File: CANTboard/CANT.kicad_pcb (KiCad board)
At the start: 2 copper layers, 20 x 50 mm, 25 parts, among them P1 SWD, P2 CAN, P3 USB, U1 STM32F042C6T6, U2 MCP2562-E/SN, U3 LD1117S33TR, U4 74LVC1G66

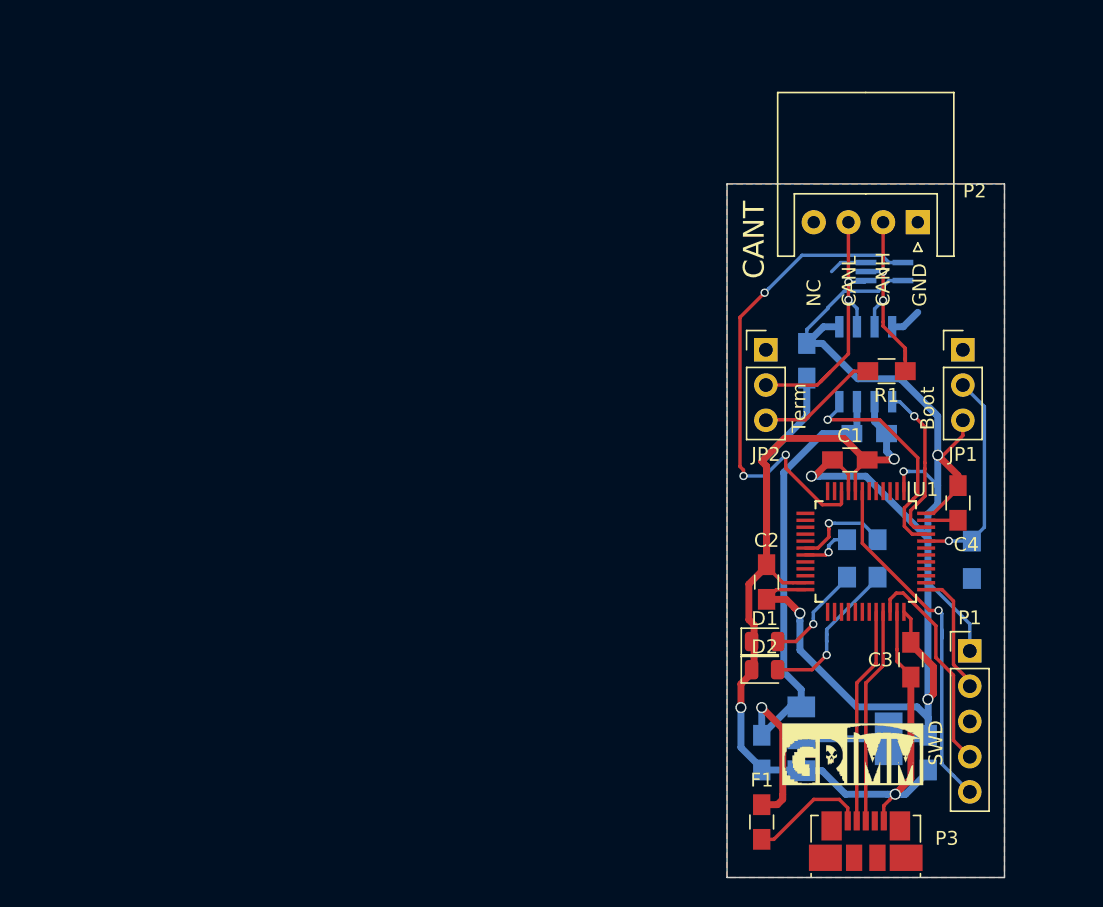
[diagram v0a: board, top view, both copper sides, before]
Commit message: Laid out CANT board based on STM32H7
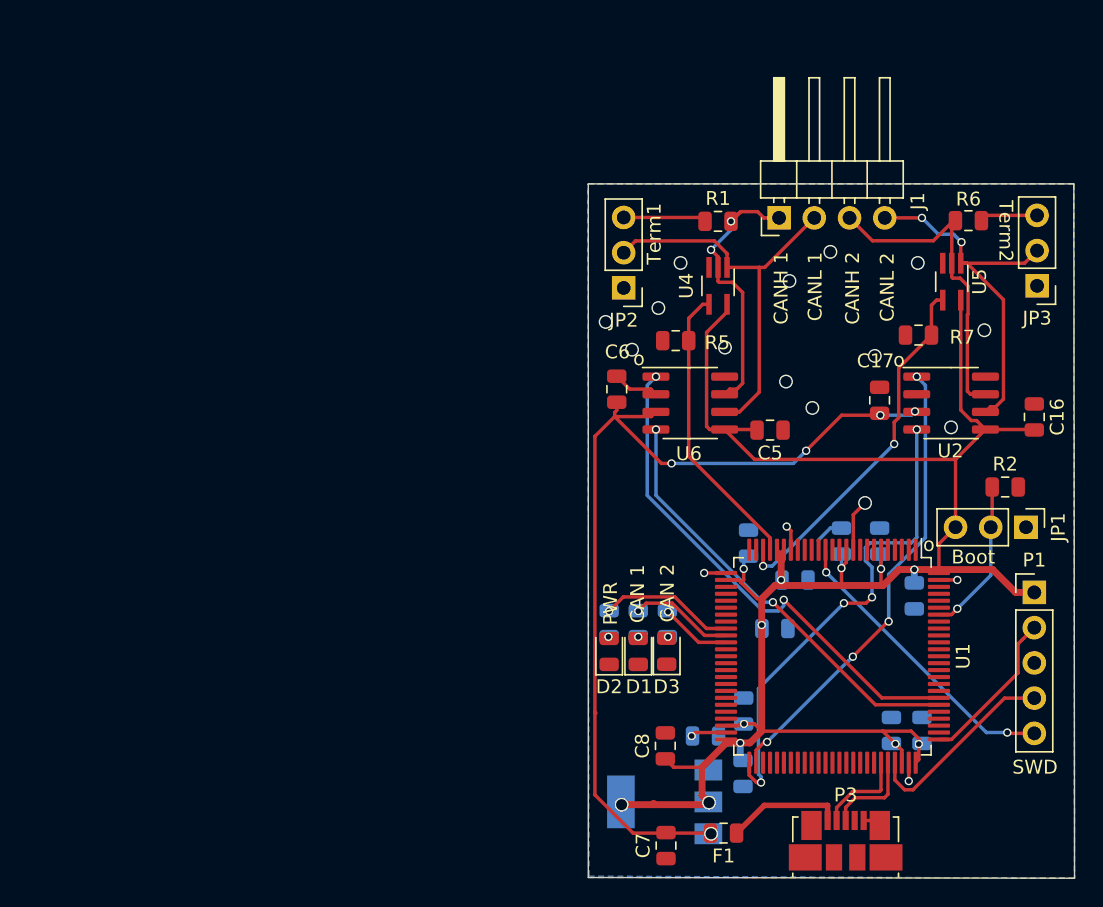
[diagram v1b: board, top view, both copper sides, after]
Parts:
- removed G***: LOGO, LOGO
- removed P2: CAN, Connectors_JST:JST_XH_S04B-XH-A_04x2.50mm_Angled
- added C10: 2.2uF, Capacitor_SMD:C_0805_2012Metric, B.Cu at (133.6, 116.9)
- added C11: 100nF, Capacitor_SMD:C_0805_2012Metric, B.Cu at (122.9, 120.0)
- added C12: 100nF, Capacitor_SMD:C_0805_2012Metric, B.Cu at (135.8, 116.9)
- added C13: 100nF, Capacitor_SMD:C_0805_2012Metric, B.Cu at (135.2, 107.2)
- added C14: 100nF, Capacitor_SMD:C_0805_2012Metric, B.Cu at (126.7, 106.0)
- added C15: 1uF, Capacitor_SMD:C_0805_2012Metric, B.Cu at (125.2, 109.5)
- added C16: 100nF, Capacitor_SMD:C_0805_2012Metric, F.Cu at (143.9, 94.3)
- added C17: 100nF, Capacitor_SMD:C_0805_2012Metric, F.Cu at (132.8, 93.1)
- added C9: 2.2uF, Capacitor_SMD:C_0805_2012Metric, B.Cu at (123.0, 115.5)
- added D3: LED-RED, LED_SMD:LED_0805_2012Metric, F.Cu at (117.4, 111.2)
- added J1: Screw_Terminal_01x04, Connector_PinHeader_2.54mm:PinHeader_1x04_P2.54mm_Horizontal, F.Cu at (125.5, 80.0)
- added JP3: Jumper_NC_Dual, Connector_PinHeader_2.54mm:PinHeader_1x03_P2.54mm_Vertical, F.Cu at (144.1, 84.8)
- added R5: 4.7K, Resistor_SMD:R_0805_2012Metric, F.Cu at (118.0, 88.8)
- added R6: 120, Resistor_SMD:R_0805_2012Metric, F.Cu at (139.2, 80.2)
- added R7: 4.7K, Resistor_SMD:R_0805_2012Metric, F.Cu at (135.6, 88.4)
- added R8: 68, Resistor_SMD:R_0805_2012Metric, B.Cu at (117.5, 109.2)
- added U5: 74LVC1G66, Package_TO_SOT_SMD:SOT-353_SC-70-5_Handsoldering, F.Cu at (137.9, 84.5)
- added U6: MCP2558FD-xSN, Package_SO:SOIC-8_3.9x4.9mm_P1.27mm, F.Cu at (119.1, 93.3)
- C1, C2, C4: value 0.1uF -> 100nF; footprint Capacitors_SMD:C_0805_HandSoldering -> Capacitor_SMD:C_0805_2012Metric; moved to B.Cu
- C3: value 1uF -> 4.7uF; footprint Capacitors_SMD:C_0805_HandSoldering -> Capacitor_SMD:C_0805_2012Metric; moved to B.Cu
- C5, C6: value 0.1uF -> 100nF; footprint Capacitors_SMD:C_0805_HandSoldering -> Capacitor_SMD:C_0805_2012Metric; moved to F.Cu
- C7, C8: footprint Capacitors_SMD:C_0805_HandSoldering -> Capacitor_SMD:C_0805_2012Metric; moved to F.Cu
- F1: footprint Capacitors_SMD:C_0805_HandSoldering -> Capacitor_SMD:C_0805_2012Metric
- JP1, JP2: footprint Pin_Headers:Pin_Header_Straight_1x03_Pitch2.54mm -> Connector_PinHeader_2.54mm:PinHeader_1x03_P2.54mm_Vertical
- P1: footprint Pin_Headers:Pin_Header_Straight_1x05_Pitch2.54mm -> Connector_PinHeader_2.54mm:PinHeader_1x05_P2.54mm_Vertical
- P3: footprint Connectors_Molex:USB_Micro-B_Molex_47346-0001 -> Connector_USB:USB_Micro-B_Molex_47346-0001
- R1: footprint Resistors_SMD:R_0805_HandSoldering -> Resistor_SMD:R_0805_2012Metric
- R2: footprint Resistors_SMD:R_0805_HandSoldering -> Resistor_SMD:R_0805_2012Metric; moved to F.Cu
- R3, R4: value R -> 68; footprint Resistors_SMD:R_0805_HandSoldering -> Resistor_SMD:R_0805_2012Metric
- U1: value STM32F042C6T6 -> STM32H743VITx; footprint Housings_QFP:LQFP-48_7x7mm_Pitch0.5mm -> Package_QFP:LQFP-100_14x14mm_P0.5mm
- U2: value MCP2562-E/SN -> MCP2558FD-xSN; footprint Housings_SOIC:SOIC-8_3.9x4.9mm_Pitch1.27mm -> Package_SO:SOIC-8_3.9x4.9mm_P1.27mm; moved to F.Cu
- U4: moved to F.Cu
- moved R4 19.9 mm to (113.2, 109.2)
- moved C8 19.0 mm to (117.3, 118.0), turned to 90 degrees
- moved R1 16.3 mm to (121.1, 80.2)
- moved C3 15.8 mm to (120.2, 117.3), turned to 180 degrees
- moved R3 15.8 mm to (115.3, 109.2)
- moved C4 15.4 mm to (123.3, 103.4), turned to 90 degrees
- moved C6 13.9 mm to (113.8, 92.3), turned to 270 degrees
- moved U3 13.8 mm to (117.2, 122.0), turned to 180 degrees
- moved JP1 13.6 mm to (143.3, 102.2), turned to 270 degrees
- moved U4 12.0 mm to (121.1, 84.8), turned to 270 degrees
- moved D2 11.3 mm to (113.2, 111.2), turned to 90 degrees
- moved JP2 11.2 mm to (114.3, 85.0), turned to 180 degrees
- moved C7 9.62 mm to (117.3, 125.2)
- moved D1 9.14 mm to (115.3, 111.2), turned to 90 degrees
- moved U1 7.92 mm to (129.3, 111.5)
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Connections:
- C5 pad 2: VBUS -> VCC
- C6 pad 2: VCC -> VBUS
- JP1 pad 1: Net-(JP1-Pad1) -> (no net)
- JP2 pad 1: Net-(JP2-Pad1) -> (no net)
- JP2 pad 2: CAN_L -> CAN1_L
- P3 pad 4: Net-(P3-Pad4) -> (no net)
- R1 pad 2: CAN_H -> CAN1_H
- R3 pad 2: LED_ACT -> LED_ACT1
- R4 pad 2: LED_PWR -> LED_PWR1
- U1 pad 1: VCC -> (no net)
- U1 pad 10: CAN_SHORT -> GND
- U1 pad 11: Net-(U1-Pad11) -> VCC
- U1 pad 12: Net-(U1-Pad12) -> (no net)
- U1 pad 13: Net-(U1-Pad13) -> (no net)
- U1 pad 14: Net-(U1-Pad14) -> /NRST
- U1 pad 15: Net-(U1-Pad15) -> (no net)
- U1 pad 16: Net-(U1-Pad16) -> (no net)
- U1 pad 17: Net-(U1-Pad17) -> (no net)
- U1 pad 18: LED_PWR -> (no net)
- U1 pad 19: LED_ACT -> GND
- U1 pad 2: Net-(U1-Pad2) -> (no net)
- U1 pad 20: Net-(U1-Pad20) -> VCC
- U1 pad 21: Net-(U1-Pad21) -> VCC
- U1 pad 22: Net-(U1-Pad22) -> CAN1_SHORT
- U1 pad 23: GND -> CAN2_SHORT
- U1 pad 24: VCC -> (no net)
- U1 pad 25: Net-(U1-Pad25) -> (no net)
- U1 pad 26: Net-(U1-Pad26) -> GND
- U1 pad 27: Net-(U1-Pad27) -> VCC
- U1 pad 28: Net-(U1-Pad28) -> (no net)
- U1 pad 29: Net-(U1-Pad29) -> (no net)
- U1 pad 3: Net-(U1-Pad3) -> (no net)
- U1 pad 30: Net-(U1-Pad30) -> (no net)
- U1 pad 31: Net-(U1-Pad31) -> (no net)
- U1 pad 32: /USB_DM -> (no net)
- U1 pad 33: /USB_DP -> (no net)
- U1 pad 34: /SWDIO -> LED_PWR1
- U1 pad 35: GND -> LED_ACT1
- U1 pad 36: VCC -> LED_ACT2
- U1 pad 37: /SWCLK -> (no net)
- U1 pad 38: Net-(U1-Pad38) -> (no net)
- U1 pad 39: Net-(U1-Pad39) -> (no net)
- U1 pad 4: Net-(U1-Pad4) -> (no net)
- U1 pad 40: Net-(U1-Pad40) -> (no net)
- U1 pad 41: Net-(U1-Pad41) -> (no net)
- U1 pad 42: Net-(U1-Pad42) -> (no net)
- U1 pad 43: Net-(U1-Pad43) -> (no net)
- U1 pad 44: BOOT0 -> (no net)
- U1 pad 45: /CAN_RX -> (no net)
- U1 pad 46: /CAN_TX -> (no net)
- U1 pad 47: GND -> (no net)
- U1 pad 5: Net-(U1-Pad5) -> (no net)
- U1 pad 6: Net-(U1-Pad6) -> VCC
- U1 pad 7: /NRST -> (no net)
- U1 pad 8: GND -> (no net)
- U1 pad 9: VCC -> (no net)
- U2 pad 1: /CAN_TX -> /CAN2_TX
- U2 pad 4: /CAN_RX -> /CAN2_RX
- U2 pad 6: CAN_L -> CAN2_L
- U2 pad 7: CAN_H -> CAN2_H
- U4 pad 1: CAN_L -> CAN1_L
- U4 pad 2: CAN_H -> CAN1_H
- U4 pad 4: CAN_SHORT -> CAN1_SHORT
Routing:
- net GND: track 97.3 -> 19.1 mm, vias 3 -> 19
- net /CAN1_TX: track 0.00 -> 36.8 mm, vias 0 -> 2
- net CAN_SHORT: track 36.0 -> 0.00 mm, vias 3 -> 0
- net /CAN2_RX: track 0.00 -> 35.4 mm, vias 0 -> 4
- net /CAN2_TX: track 0.00 -> 33.3 mm, vias 0 -> 4
- net /CAN1_RX: track 0.00 -> 31.4 mm, vias 0 -> 2
- net CAN1_L: track 0.00 -> 29.0 mm
- net CAN2_L: track 0.00 -> 26.7 mm, vias 0 -> 2
- net CAN2_SHORT: track 0.00 -> 26.4 mm, vias 0 -> 2
- net VBUS: track 40.8 -> 66.3 mm, vias 1 -> 5
- net VCC: track 120.4 -> 144.9 mm, vias 5 -> 12
- net CAN2_H: track 0.00 -> 24.5 mm
- net CAN1_SHORT: track 0.00 -> 21.0 mm
- net CAN_L: track 20.8 -> 0.00 mm, vias 2 -> 0
- net CAN1_H: track 0.00 -> 20.3 mm, vias 0 -> 2
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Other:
- board size 20 x 50 mm -> 35.1 x 50 mm
- board text added: "CAN 1"
- board text added: "CAN 2"
- board text added: "CANH 1"
- board text added: "CANH 2"
- board text added: "CANL 1"
- board text added: "CANL 2"
- board text added: "PWR"
- board text added: "Term1"
- board text added: "Term2"
- board text added: "Version: 1.0"
- board text added: "https://github.com/bitbane/CANT @b1tbane thb@grimm-co.com"
- board text added: "o"
- board text removed: "CANH"
- board text removed: "CANL"
- board text removed: "CANT"
- board text removed: "GND"
- board text removed: "NC"
- board text removed: "Term"
- board text removed: "Version: 3.0"
- board text removed: "https://github.com/bitbane/CANT @b1tbane"

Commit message: Added logo, because how could I forget that
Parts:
- added G***: LOGO, KiCad:Logo, B.Cu at (129.2, 86.8)
- moved F1 2.45 mm to (124.0, 124.3)
- moved R8 2.15 mm to (117.3, 107.0)
- moved R3 2.10 mm to (115.4, 107.1)
- moved R4 2.10 mm to (113.3, 107.1)
- moved D3 0.56 mm to (117.4, 111.8)
- moved D2 0.55 mm to (113.3, 111.8)
- moved D1 0.55 mm to (115.3, 111.8)
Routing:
- net GND: track 19.1 -> 43.9 mm, vias 19 -> 12
- net VCC: track 144.9 -> 155.2 mm, vias 12 -> 9
- net VBUS: track 66.3 -> 72.2 mm, vias 5 -> 3
- net LED_ACT1: track 7.53 -> 10.5 mm
- net Net-(D3-Pad2): track 0.00 -> 2.85 mm
- net Net-(D1-Pad2): track 0.00 -> 2.80 mm
- net Net-(D2-Pad2): track 0.00 -> 2.78 mm
- net LED_ACT2: track 5.09 -> 7.85 mm
- net LED_PWR1: track 9.79 -> 12.3 mm
- net Net-(F1-Pad1): track 8.48 -> 6.03 mm
- net /CAN2_TX: track 33.3 -> 35.5 mm
- net /CAN1_TX: track 36.8 -> 38.4 mm

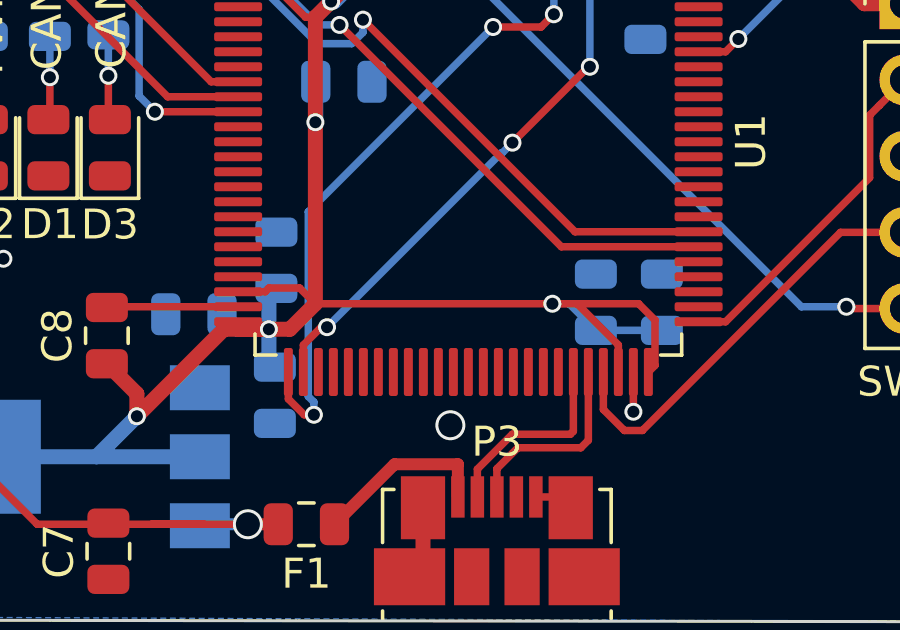
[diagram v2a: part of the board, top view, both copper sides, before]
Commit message: Fix VCAP connection issue - apparently, these are not supposed to be connected to VDD
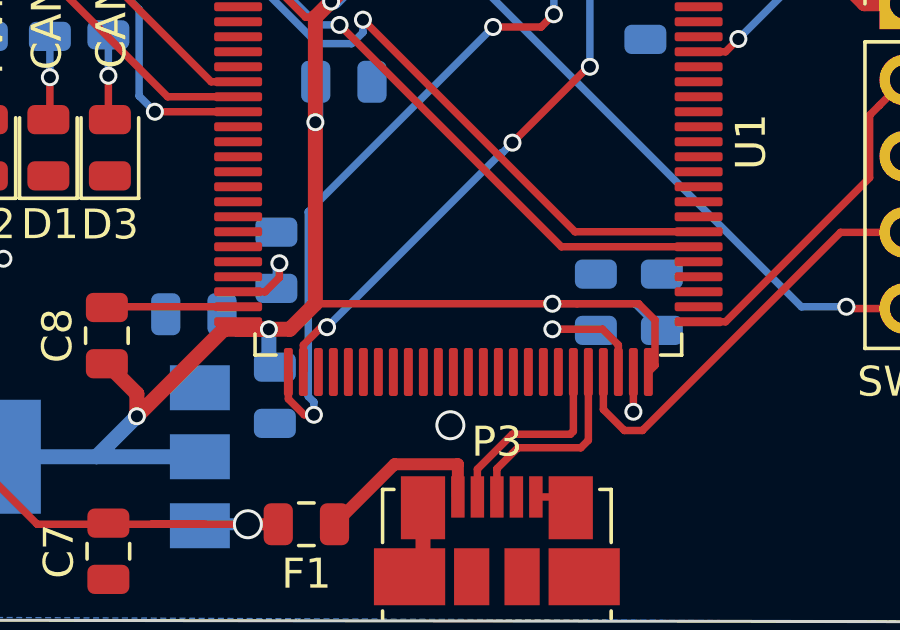
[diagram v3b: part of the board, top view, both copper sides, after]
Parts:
- removed G***: LOGO, KiCad:Logo
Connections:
- C10 pad 1: VCC -> Net-(C10-Pad1)
- C9 pad 1: VCC -> Net-(C9-Pad1)
- U1 pad 48: VCC -> Net-(C9-Pad1)
- U1 pad 73: VCC -> Net-(C10-Pad1)
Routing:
- net VCC: track 155.2 -> 147.9 mm
- net Net-(C10-Pad1): track 0.00 -> 4.78 mm, vias 0 -> 1
- net Net-(C9-Pad1): track 0.00 -> 3.21 mm, vias 0 -> 1
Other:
- board text added: "https://github.com/bitbane/CANT Tim Brom Managing Senior Security Researcher @b1tbane thb@grimm-co.com"
- board text removed: "https://github.com/bitbane/CANT @b1tbane thb@grimm-co.com"

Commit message: Starting design of unified board
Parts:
- added C18: 26pF, Capacitor_SMD:C_0805_2012Metric, F.Cu at (105.7, 98.8)
- added C19: 26pF, Capacitor_SMD:C_0805_2012Metric, F.Cu at (109.5, 98.8)
- added C20: 100nF, Capacitor_SMD:C_0805_2012Metric, F.Cu at (134.1, 97.3)
- added J2: Conn_02x08_Odd_Even, Connector_PinHeader_2.54mm:PinHeader_2x08_P2.54mm_Vertical, F.Cu at (126.5, 81.0)
- added R9: 100K, Resistor_SMD:R_0805_2012Metric, F.Cu at (137.7, 97.3)
- added SW1: SW_SPST, Button_Switch_SMD:SW_SPST_PTS645, F.Cu at (135.1, 88.9)
- added U7: USBLC6-2SC6, Package_TO_SOT_SMD:SOT-23-6, F.Cu at (97.0, 75.7)
- added Y1: Crystal, Crystal:Crystal_SMD_HC49-SD, F.Cu at (107.7, 103.9)
- C1, C10, C11, C12, C13, C14, C15, C2, C3, C4, C9, R3, R4, R8: moved to F.Cu
- J1: footprint Connector_PinHeader_2.54mm:PinHeader_1x04_P2.54mm_Horizontal -> TerminalBlock_Phoenix:TerminalBlock_Phoenix_PT-1,5-4-3.5-H_1x04_P3.50mm_Horizontal
- U3: footprint TO_SOT_Packages_SMD:SOT-223 -> Package_TO_SOT_SMD:SOT-223; moved to F.Cu
- moved JP3 70.0 mm to (75.9, 100.8), turned to 0 degrees
- moved R6 63.6 mm to (79.8, 102.9), turned to 0 degrees
- moved C16 56.4 mm to (89.7, 78.7), turned to 180 degrees
- moved P3 54.9 mm to (111.8, 73.2), turned to 180 degrees
- moved U5 54.1 mm to (84.3, 91.4), turned to 0 degrees
- moved R7 51.6 mm to (84.3, 94.2)
- moved D1 51.4 mm to (75.9, 78.7), turned to 0 degrees
- moved C10 50.7 mm to (102.6, 76.7)
- moved C7 49.8 mm to (126.5, 76.2), turned to 90 degrees
- moved J1 49.4 mm to (76.2, 82.5), turned to 270 degrees
- moved U3 48.5 mm to (121.2, 73.7), turned to 90 degrees
- moved F1 47.7 mm to (114.8, 77.5), turned to 0 degrees
- moved C8 47.3 mm to (126.5, 71.6)
- moved R3 47.1 mm to (80.0, 75.9), turned to 0 degrees
- moved U2 46.2 mm to (91.7, 92.5), turned to 180 degrees
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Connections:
- J1 pad 1: CAN1_H -> CAN1_L
- J1 pad 2: CAN1_L -> CAN1_H
- J1 pad 3: CAN2_H -> CAN2_L
- J1 pad 4: CAN2_L -> CAN2_H
- JP1 pad 1: (no net) -> Net-(JP1-Pad1)
- JP2 pad 1: (no net) -> Net-(JP2-Pad1)
- JP3 pad 1: (no net) -> Net-(JP3-Pad1)
- P3 pad 4: (no net) -> Net-(P3-Pad4)
- U1 pad 1: (no net) -> Net-(U1-Pad1)
- U1 pad 12: (no net) -> Net-(C18-Pad2)
- U1 pad 13: (no net) -> Net-(C19-Pad1)
- U1 pad 15: (no net) -> Net-(U1-Pad15)
- U1 pad 16: (no net) -> Net-(U1-Pad16)
- U1 pad 17: (no net) -> Net-(U1-Pad17)
- U1 pad 18: (no net) -> Net-(U1-Pad18)
- U1 pad 2: (no net) -> Net-(U1-Pad2)
- U1 pad 22: CAN1_SHORT -> Net-(U1-Pad22)
- U1 pad 23: CAN2_SHORT -> Net-(U1-Pad23)
- U1 pad 24: (no net) -> Net-(U1-Pad24)
- U1 pad 25: (no net) -> Net-(U1-Pad25)
- U1 pad 28: (no net) -> Net-(U1-Pad28)
- U1 pad 29: (no net) -> Net-(U1-Pad29)
- U1 pad 3: (no net) -> Net-(U1-Pad3)
- U1 pad 30: (no net) -> Net-(U1-Pad30)
- U1 pad 31: (no net) -> Net-(U1-Pad31)
- U1 pad 32: (no net) -> Net-(U1-Pad32)
- U1 pad 33: (no net) -> Net-(U1-Pad33)
- U1 pad 37: (no net) -> Net-(U1-Pad37)
- U1 pad 38: (no net) -> Net-(J2-Pad15)
- U1 pad 39: (no net) -> Net-(J2-Pad13)
- U1 pad 4: (no net) -> Net-(U1-Pad4)
- U1 pad 40: (no net) -> Net-(J2-Pad11)
- U1 pad 41: (no net) -> Net-(J2-Pad9)
- U1 pad 42: (no net) -> Net-(J2-Pad7)
- U1 pad 43: (no net) -> Net-(J2-Pad5)
- U1 pad 44: (no net) -> Net-(J2-Pad3)
- U1 pad 45: (no net) -> Net-(J2-Pad1)
- U1 pad 46: (no net) -> Net-(U1-Pad46)
- U1 pad 47: (no net) -> Net-(U1-Pad47)
- U1 pad 5: (no net) -> Net-(U1-Pad5)
- U1 pad 51: /CAN2_RX -> Net-(U1-Pad51)
- U1 pad 52: /CAN2_TX -> Net-(U1-Pad52)
- U1 pad 53: (no net) -> Net-(U1-Pad53)
- U1 pad 54: (no net) -> Net-(U1-Pad54)
- U1 pad 55: (no net) -> Net-(U1-Pad55)
- U1 pad 56: (no net) -> Net-(U1-Pad56)
- U1 pad 57: (no net) -> Net-(U1-Pad57)
- U1 pad 58: (no net) -> Net-(U1-Pad58)
- U1 pad 59: (no net) -> Net-(U1-Pad59)
- U1 pad 60: (no net) -> Net-(U1-Pad60)
- U1 pad 61: (no net) -> Net-(U1-Pad61)
- U1 pad 62: (no net) -> Net-(U1-Pad62)
- U1 pad 63: (no net) -> Net-(U1-Pad63)
- U1 pad 64: (no net) -> Net-(U1-Pad64)
- U1 pad 65: (no net) -> Net-(U1-Pad65)
- U1 pad 66: (no net) -> Net-(U1-Pad66)
- U1 pad 67: (no net) -> Net-(U1-Pad67)
- U1 pad 68: (no net) -> Net-(U1-Pad68)
- U1 pad 69: (no net) -> Net-(U1-Pad69)
- U1 pad 7: (no net) -> Net-(U1-Pad7)
- U1 pad 77: (no net) -> Net-(U1-Pad77)
- U1 pad 78: (no net) -> Net-(U1-Pad78)
- U1 pad 79: (no net) -> Net-(U1-Pad79)
- U1 pad 8: (no net) -> Net-(U1-Pad8)
- U1 pad 80: (no net) -> Net-(U1-Pad80)
- U1 pad 81: /CAN1_RX -> Net-(U1-Pad81)
- U1 pad 82: /CAN1_TX -> Net-(U1-Pad82)
- U1 pad 83: (no net) -> Net-(U1-Pad83)
- U1 pad 84: (no net) -> Net-(U1-Pad84)
- U1 pad 85: (no net) -> Net-(U1-Pad85)
- U1 pad 86: (no net) -> Net-(U1-Pad86)
- U1 pad 87: (no net) -> Net-(U1-Pad87)
- U1 pad 88: (no net) -> Net-(U1-Pad88)
- U1 pad 89: (no net) -> Net-(U1-Pad89)
- U1 pad 9: (no net) -> Net-(U1-Pad9)
- U1 pad 90: (no net) -> CAN2_SHORT
- U1 pad 91: (no net) -> CAN2_RX
- U1 pad 92: (no net) -> CAN2_TX
- U1 pad 93: (no net) -> CAN1_SHORT
- U1 pad 95: (no net) -> CAN1_RX
- U1 pad 96: (no net) -> CAN1_TX
- U1 pad 97: (no net) -> Net-(U1-Pad97)
- U1 pad 98: (no net) -> Net-(U1-Pad98)
- U2 pad 1: /CAN2_TX -> CAN2_TX
- U2 pad 4: /CAN2_RX -> CAN2_RX
- U6 pad 1: /CAN1_TX -> CAN1_TX
- U6 pad 4: /CAN1_RX -> CAN1_RX
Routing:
- net VCC: track 147.9 -> 0.00 mm, vias 9 -> 0
- net VBUS: track 72.2 -> 0.00 mm, vias 3 -> 0
- net GND: track 43.9 -> 0.00 mm, vias 12 -> 0
- net /CAN1_TX: track 38.4 -> 0.00 mm, vias 2 -> 0
- net /CAN2_TX: track 35.5 -> 0.00 mm, vias 4 -> 0
- net /CAN2_RX: track 35.4 -> 0.00 mm, vias 4 -> 0
- net /CAN1_RX: track 31.4 -> 0.00 mm, vias 2 -> 0
- net CAN2_L: track 26.7 -> 0.00 mm, vias 2 -> 0
- net CAN2_SHORT: track 26.4 -> 0.00 mm, vias 2 -> 0
- net CAN2_H: track 24.5 -> 0.00 mm
- net CAN1_L: track 29.0 -> 7.16 mm
- net /NRST: track 21.5 -> 0.00 mm, vias 2 -> 0
- net CAN1_SHORT: track 21.0 -> 0.00 mm
- net /SWDIO: track 14.3 -> 0.00 mm
- net CAN1_H: track 20.3 -> 7.62 mm, vias 2 -> 0
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- added copper zone on B.Cu, net VCC
- removed copper zone on B.Cu, net GND
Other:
- board size 35.1 x 50 mm -> 67.8 x 45.5 mm
- board text added: "CAN1"
- board text added: "CAN2"
- board text added: "HI"
- board text added: "LO"
- board text removed: "1. 3.3v 2. SWCLK 3. GND 4. SWDIO 5. NRST"
- board text removed: "Boot"
- board text removed: "CAN 1"
- board text removed: "CAN 2"
- board text removed: "CANH 1"
- board text removed: "CANH 2"
- board text removed: "CANL 1"
- board text removed: "CANL 2"
- board text removed: "PWR"
- board text removed: "SWD"
- board text removed: "Term1"
- board text removed: "Term2"
- board text removed: "Version: 1.0"
- board text removed: "https://github.com/bitbane/CANT Tim Brom Managing Senior Security Researcher @b1tbane thb@grimm-co.com"
- board text removed: "o"
